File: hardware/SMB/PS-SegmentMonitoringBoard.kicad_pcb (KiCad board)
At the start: 4 copper layers, 85 x 80 mm, 121 parts, among them IC1 BQ79616PAPR, J1 voltTapsConn, J2 highSideConn, J3 lowSideConn, J4 thermsConn, Q1 ZXTN4004KTC

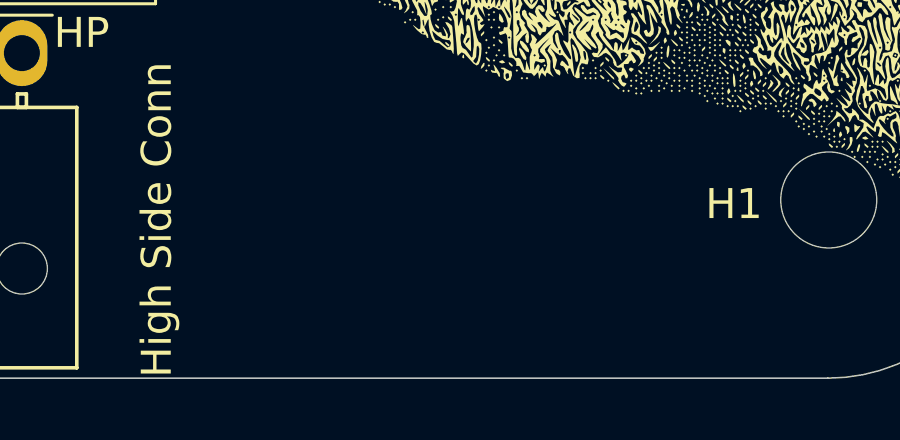
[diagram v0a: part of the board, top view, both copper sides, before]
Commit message: added two wolves n new gerbers
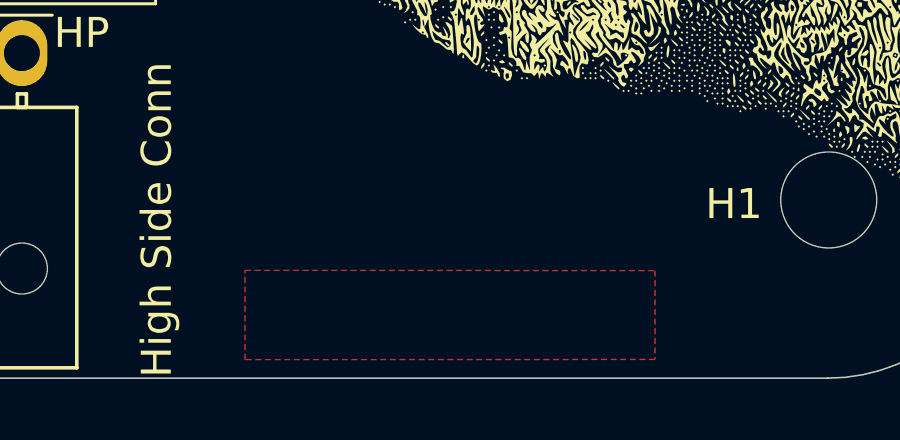
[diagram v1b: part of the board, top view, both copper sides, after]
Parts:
- added G***: LOGO, LOGO, B.Cu at (99.8, 87.0)
- moved G*** 32.4 mm to (117.8, 105.5)
- moved G*** 14.3 mm to (138.8, 83.6)
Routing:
- added copper zone on F.Cu, net (none)
